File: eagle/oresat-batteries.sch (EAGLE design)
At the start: 312 parts, among them J1 J-SAMTEC-TFM-120-X1-XXX-D-RA, J4 ORESAT-DEBUG-CONNECTOR-ALL, Q1 DMP2240UDM, Q10 NTR4101, Q11 PMV45EN, Q12 Si7625DN, Q13 Si7625DN, Q14 NTR4101, Q15 NTR4101, Q16 Si7625DN, Q17 Si7625DN, Q18 Si7625DN, Q19 Si7625DN, Q2 PMV45EN, Q22 PMV45EN, Q23 NTR4101, Q24 PM45VEN, Q25 PM45VEN, Q26 PM45VEN, Q27 PM45VEN, Q28 NTR4101, Q29 PM45VEN, Q3 DMP3050LVT-7, Q30 Si7625DN, Q31 Si7625DN, Q32 NTR4101, Q33 NTR4101, Q34 Si7625DN, Q35 Si7625DN, Q36 Si7625DN, Q37 Si7625DN, Q4 DMP3050LVT-7, Q40 PM45VEN, Q41 NTR4101, Q42 DMP2240UDM, Q43 DMP2240UDM, Q44 PMV45EN, Q45 FDMQ86530L_2-GATES, Q5 PMV45EN, Q6 PM45VEN, Q7 PM45VEN, Q8 PM45VEN, Q9 PM45VEN, U1 MAX7310ATE, U10 LTC4412, U11 LTC4412, U12 MAX17205G, U13 S-8209AAA-T8T1U, U14 S-8209AAA-T8T1U, U15 LTC4412, U16 LTC4412, U17 MAX17205G, U2 MIC842LYC5, U20 TCAN330, U21 STM32F091C, U3 MIC842LYC5, U4 MAX4211FETE, U5 TPS62111RSA, U8 S-8209AAA-T8T1U, U9 S-8209AAA-T8T1U, X3 16MHZ-2.5x2mm

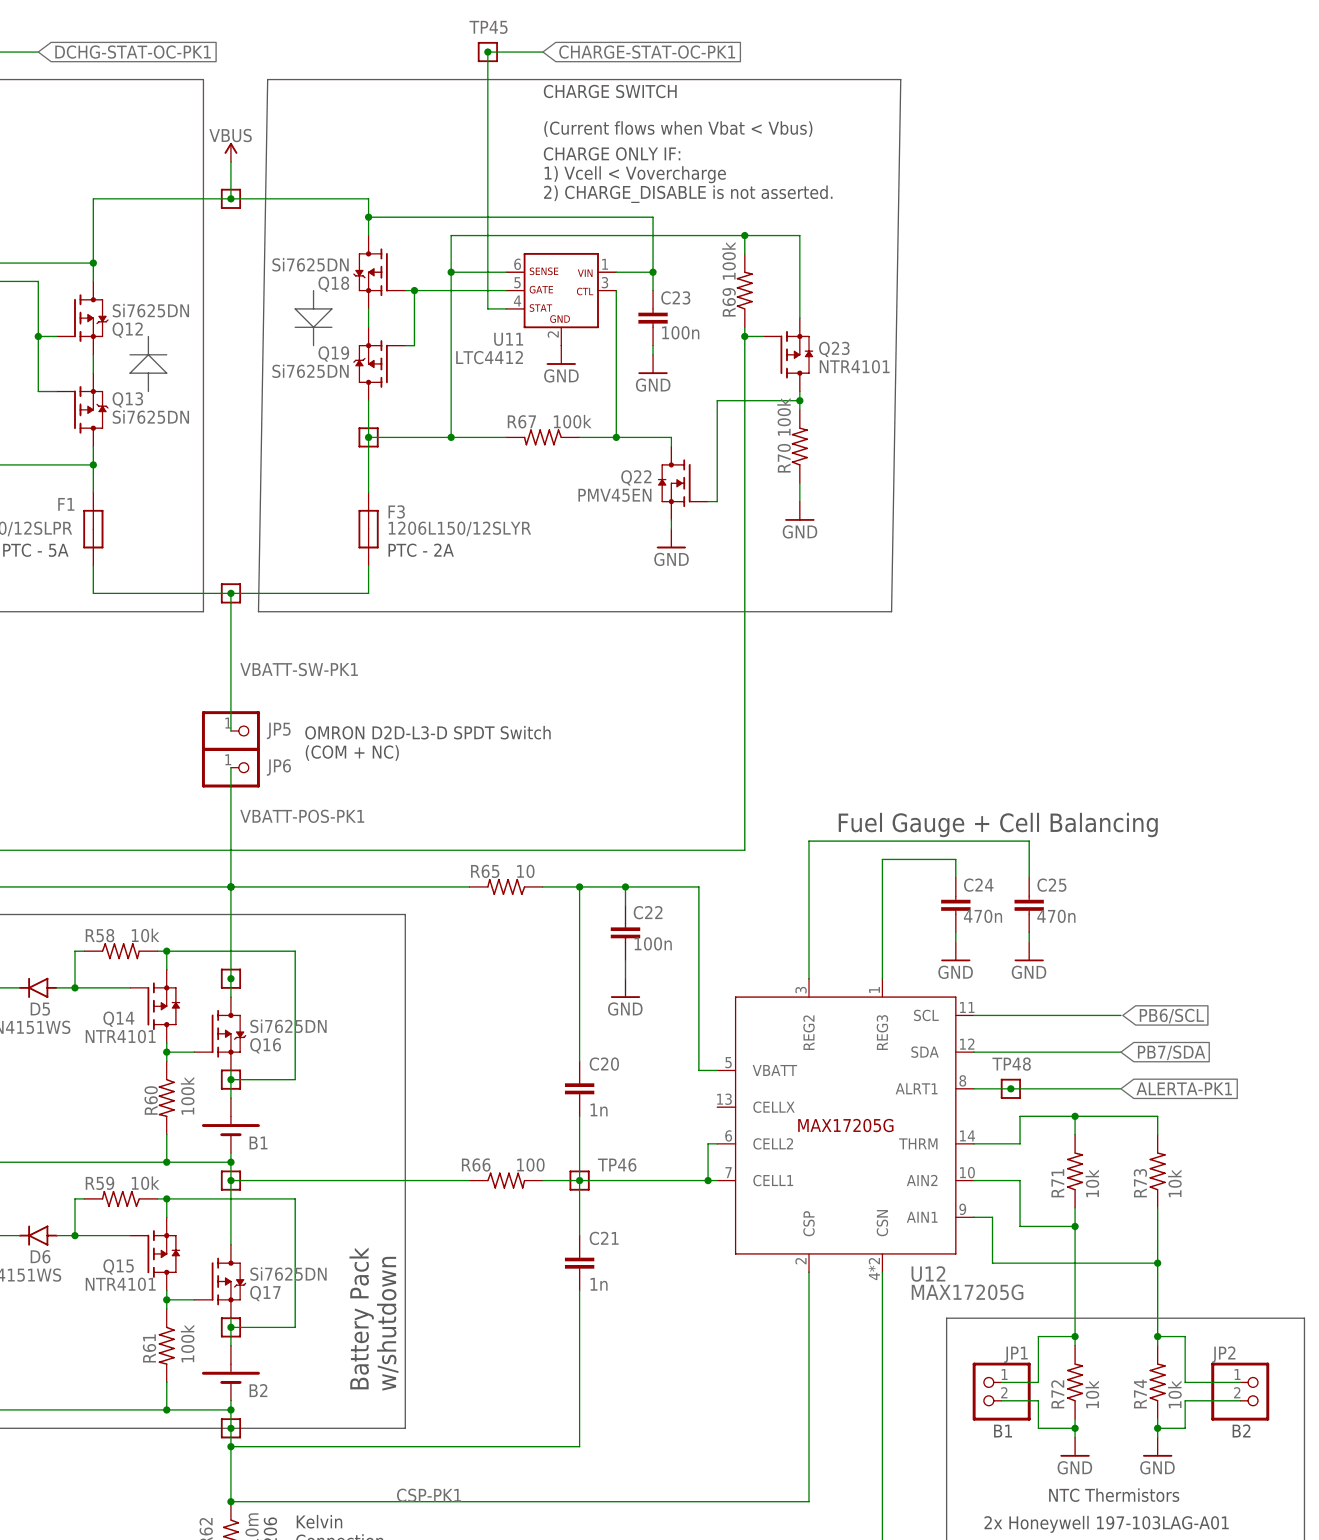
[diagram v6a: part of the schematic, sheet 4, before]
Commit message: Updated shutdown mosfet resistors to 100k after the battery failed quiescent power draw, and removed backup thermistors from the BOM.
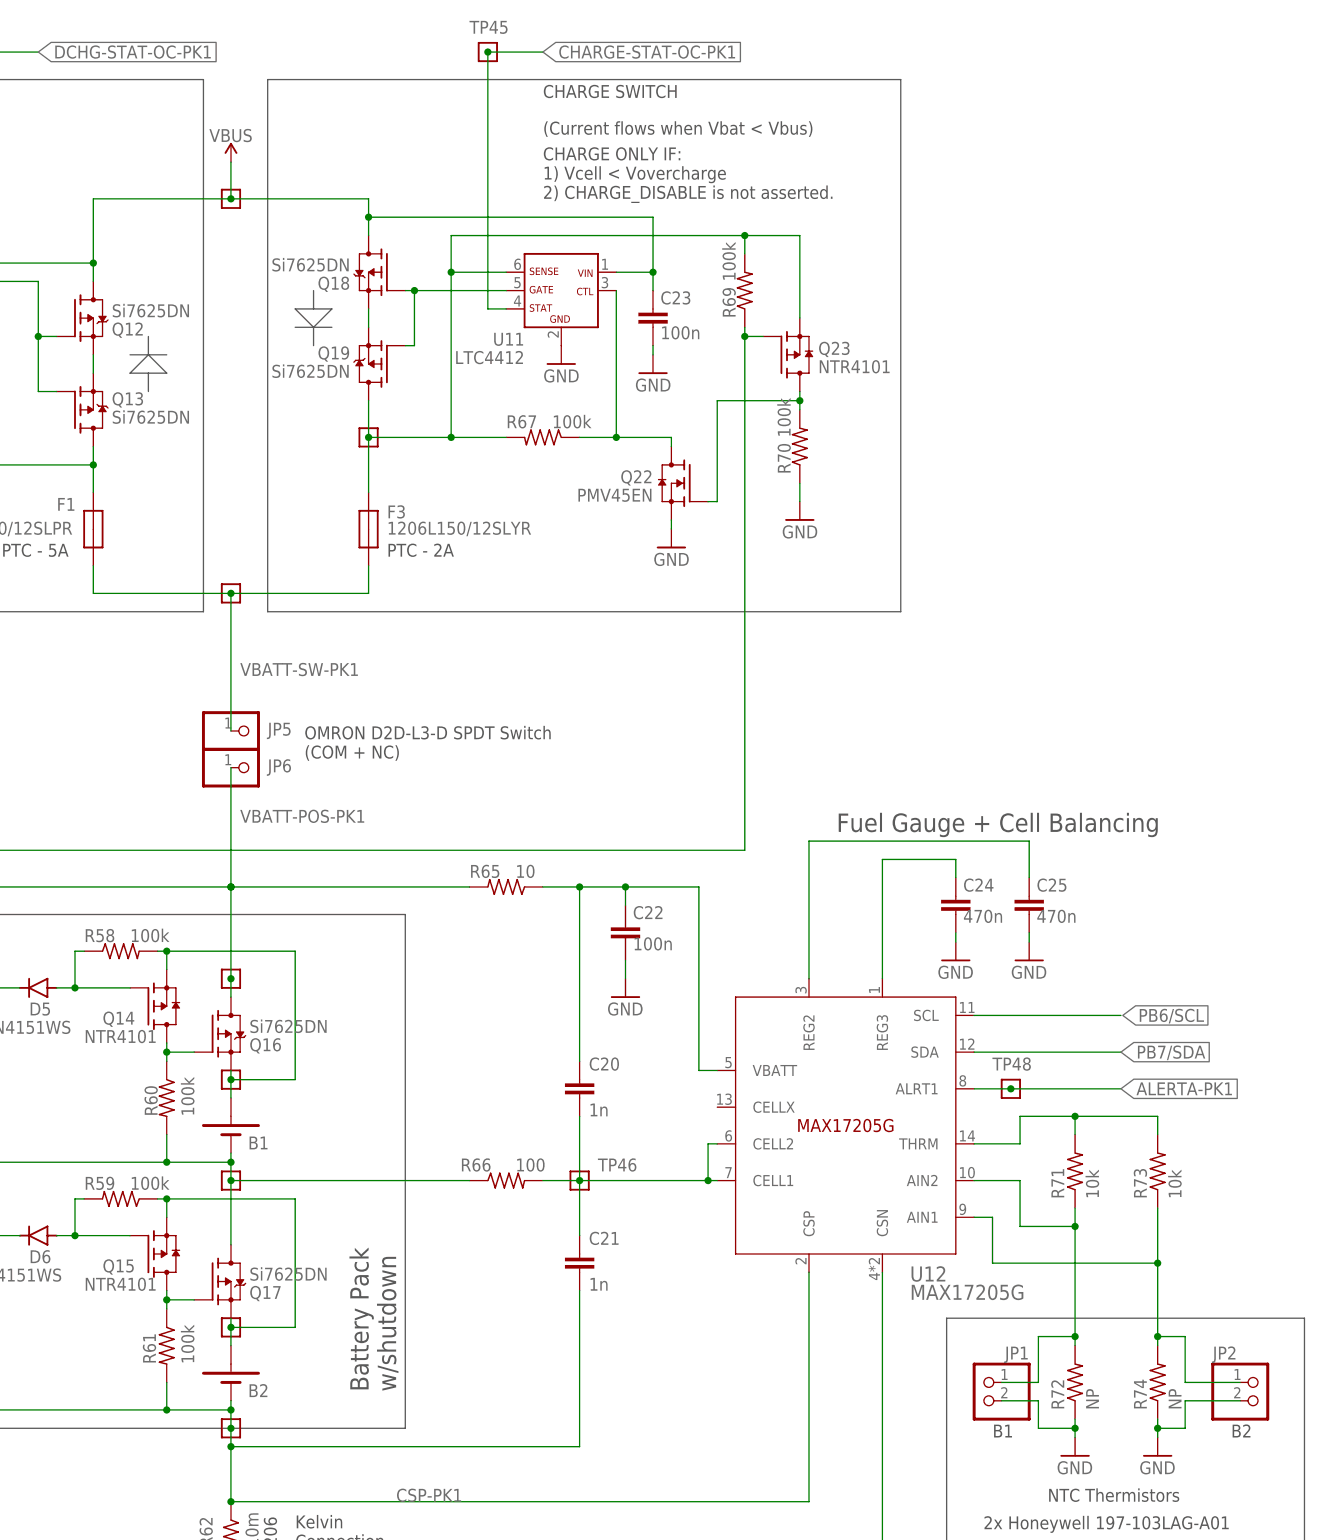
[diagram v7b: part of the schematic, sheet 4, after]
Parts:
- R102, R104, R72, R74: value 10k -> NP
- R58, R59, R88, R89: value 10k -> 100k
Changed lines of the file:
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@@
 <attribute name="MPN" value="RC0603FR-0710KL"/>
 </part>
-<part name="R72" library="oresat-rcl" deviceset="R-US_" device="0603-C-NOSILK" value="10k">
+<part name="R72" library="oresat-rcl" deviceset="R-US_" device="0603-C-NOSILK" value="NP">
 <attribute name="DIS" value="Digi-Key"/>
 <attribute name="DPN" value="311-10.0KHRCT-ND"/>
@@
 <attribute name="MPN" value="RC0603FR-0710KL"/>
 </part>
-<part name="R74" library="oresat-rcl" deviceset="R-US_" device="0603-C-NOSILK" value="10k">
+<part name="R74" library="oresat-rcl" deviceset="R-US_" device="0603-C-NOSILK" value="NP">
 <attribute name="DIS" value="Digi-Key"/>
 <attribute name="DPN" value="311-10.0KHRCT-ND"/>
@@
 <attribute name="MPN" value="1N4151WS-E3-08"/>
 </part>
-<part name="R59" library="oresat-rcl" deviceset="R-US_" device="0603-C-NOSILK" value="10k">
+<part name="R59" library="oresat-rcl" deviceset="R-US_" device="0603-C-NOSILK" value="100k">
 <attribute name="DIS" value="Digi-Key"/>
 <attribute name="DPN" value="311-1.00MHRCT-ND"/>
@@
 <attribute name="MPN" value="RC0603FR-071ML"/>
 </part>
-<part name="R58" library="oresat-rcl" deviceset="R-US_" device="0603-C-NOSILK" value="10k">
+<part name="R58" library="oresat-rcl" deviceset="R-US_" device="0603-C-NOSILK" value="100k">
 <attribute name="DIS" value="Digi-Key"/>
 <attribute name="DPN" value="311-1.00MHRCT-ND"/>
@@
 <attribute name="MPN" value="RC0603FR-0710KL"/>
 </part>
-<part name="R102" library="oresat-rcl" deviceset="R-US_" device="0603-C-NOSILK" value="10k">
+<part name="R102" library="oresat-rcl" deviceset="R-US_" device="0603-C-NOSILK" value="NP">
 <attribute name="DIS" value="Digi-Key"/>
 <attribute name="DPN" value="311-10.0KHRCT-ND"/>
@@
 <attribute name="MPN" value="RC0603FR-0710KL"/>
 </part>
-<part name="R104" library="oresat-rcl" deviceset="R-US_" device="0603-C-NOSILK" value="10k">
+<part name="R104" library="oresat-rcl" deviceset="R-US_" device="0603-C-NOSILK" value="NP">
 <attribute name="DIS" value="Digi-Key"/>
 <attribute name="DPN" value="311-10.0KHRCT-ND"/>
@@
 <attribute name="MPN" value="1N4151WS-E3-08"/>
 </part>
-<part name="R89" library="oresat-rcl" deviceset="R-US_" device="0603-C-NOSILK" value="10k">
+<part name="R89" library="oresat-rcl" deviceset="R-US_" device="0603-C-NOSILK" value="100k">
 <attribute name="DIS" value="Digi-Key"/>
 <attribute name="DPN" value="311-1.00MHRCT-ND"/>
@@
 <attribute name="MPN" value="RC0603FR-071ML"/>
 </part>
-<part name="R88" library="oresat-rcl" deviceset="R-US_" device="0603-C-NOSILK" value="10k">
+<part name="R88" library="oresat-rcl" deviceset="R-US_" device="0603-C-NOSILK" value="100k">
 <attribute name="DIS" value="Digi-Key"/>
 <attribute name="DPN" value="311-1.00MHRCT-ND"/>
@@
 <wire x1="252.73" y1="186.69" x2="154.94" y2="186.69" width="0.1524" layer="97"/>
 <wire x1="154.94" y1="186.69" x2="154.94" y2="260.35" width="0.1524" layer="97"/>
-<wire x1="261.62" y1="260.35" x2="260.35" y2="186.69" width="0.1524" layer="97"/>
+<wire x1="261.62" y1="260.35" x2="261.62" y2="186.69" width="0.1524" layer="97"/>
 <wire x1="261.62" y1="260.35" x2="349.25" y2="260.35" width="0.1524" layer="97"/>
-<wire x1="260.35" y1="186.69" x2="347.98" y2="186.69" width="0.1524" layer="97"/>
-<wire x1="349.25" y1="260.35" x2="347.98" y2="186.69" width="0.1524" layer="97"/>
+<wire x1="261.62" y1="186.69" x2="349.25" y2="186.69" width="0.1524" layer="97"/>
+<wire x1="349.25" y1="260.35" x2="349.25" y2="186.69" width="0.1524" layer="97"/>
 <text x="335.28" y="26.67" size="3.81" layer="94">OreSat battery Card - Battery Pack 1</text>
 <text x="416.56" y="6.35" size="3.81" layer="94">1.0</text>

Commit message: OreSat Battery Card v2.1
- Shrunk fastener foot prints to gain more room.
- Redid DF3 switch layouts to get the jumper wires closer to the switche's mini-contact holes.
- Added fiducials.
- Replaced quad N channel MOSFET with four N channels because the quad pack is unobtainium right now.
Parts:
- removed Q45: FDMQ86530L_2-GATES, Q-On_Semiconductor-FDMQ86530L-MOSFET-4-N-CH:FDMQ86530L_2-GATES
- added Q20, Q21, Q38, Q39: PMV45EN, Q-MOSFET-NCH-SOT23-3:N-MOSFET-SOT-23-3
- added R63, R64: 4.7k, oresat-rcl:R-US_0603-C-NOSILK
- added TP19, TP20, TP21, TP22: TEST-POINT-LARGE-SQUARE, oresat-misc:TEST-POINT-LARGE-SQUARE
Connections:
- new net I2C2_SCL: R63.1, TP19.1, U17.SCL, U21.PB13
- new net I2C2_SDA: R64.1, TP20.1, U17.SDA, U21.PB14
- new net N$88: Q20.D, Q39.S
- new net N$92: Q21.D, Q38.S
- net 3.3V: now also R63.2, R64.2
- net ALERTA-PK2: now also U21.PB12; no longer U21.PB4
- net GND: now also Q20.S, Q21.S; no longer Q45.S
- net HEATER-ON-1: now also Q21.G, Q39.G; no longer Q45.G1-3
- net HEATER-ON-2: now also Q20.G, Q38.G; no longer Q45.G2-4
- net MOARPWR: now also U21.PB15; no longer U21.PB14
- net N$64: now also Q38.D, Q39.D; no longer Q45.D
- net PB6/SCL: now also TP21.1; no longer U17.SCL
- net PB7/SDA: now also TP22.1; no longer U17.SDA
